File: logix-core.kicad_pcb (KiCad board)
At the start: 6 copper layers, 76 parts, among them J1 QSH-030-01-X-D-A-XX, J2 QSH-030-01-X-D-A-XX, J3 878321420, U1 XC7A15T-CSG325, U1 XC7A15T-FTG256, U2 MP5470GL-0000-P, U3 TPUSBLC6-4SC6, U4 FT230XQ, U5 MX25L3233FZN, U6 XC7A15T-CSG325, U8 MT41K256M16TW-107:P

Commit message: more ddr3, rules and stuff
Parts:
- R17: value R -> 100; footprint Resistor_SMD:R_0402_1005Metric_Pad0.72x0.64mm_HandSolder -> Capacitor_SMD:C_0402_1005Metric
- U1: value XC7A15T-FTG256 -> XC7A15T-CSG325; footprint Package_BGA:Xilinx_FTG256 -> Package_BGA:Xilinx_CSG325
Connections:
- R17 pad 1: /FPGA/DO.DO6+ -> +V1P2
- R17 pad 2: unconnected-(R17-Pad2) -> Net-(U1D-MGTRREF_216)
- U1 pad A10: unconnected-(U1A-IO_L3N_T0_DQS_AD1N_15-PadA10) -> (no net)
- U1 pad A12: unconnected-(U1A-IO_L5N_T0_AD9N_15-PadA12) -> (no net)
- U1 pad A13: unconnected-(U1A-IO_L7P_T1_AD2P_15-PadA13) -> (no net)
- U1 pad A14: unconnected-(U1A-IO_L7N_T1_AD2N_15-PadA14) -> (no net)
- U1 pad A15: unconnected-(U1A-IO_L9N_T1_DQS_AD3N_15-PadA15) -> (no net)
- U1 pad A16: unconnected-(U1A-VCCO_15-PadA16) -> (no net)
- U1 pad A2: (no net) -> +V1P2
- U1 pad A6: (no net) -> Net-(U1D-MGTRREF_216)
- U1 pad A8: unconnected-(U1A-IO_L2P_T0_AD8P_15-PadA8) -> (no net)
- U1 pad A9: unconnected-(U1A-IO_L2N_T0_AD8N_15-PadA9) -> (no net)
- U1 pad B10: unconnected-(U1A-IO_L4P_T0_15-PadB10) -> (no net)
- U1 pad B11: unconnected-(U1A-IO_L4N_T0_15-PadB11) -> (no net)
- U1 pad B12: unconnected-(U1A-IO_L5P_T0_AD9P_15-PadB12) -> (no net)
- U1 pad B13: unconnected-(U1A-VCCO_15-PadB13) -> (no net)
- U1 pad B14: unconnected-(U1A-IO_L8N_T1_AD10N_15-PadB14) -> (no net)
- U1 pad B15: unconnected-(U1A-IO_L9P_T1_DQS_AD3P_15-PadB15) -> (no net)
- U1 pad B16: unconnected-(U1A-IO_L10N_T1_AD11N_15-PadB16) -> (no net)
- U1 pad B4: (no net) -> +V1P0
- U1 pad B9: unconnected-(U1A-IO_L3P_T0_DQS_AD1P_15-PadB9) -> (no net)
- U1 pad C1: (no net) -> +V1P2
- U1 pad C10: unconnected-(U1A-VCCO_15-PadC10) -> (no net)
- U1 pad C11: unconnected-(U1A-IO_L11P_T1_SRCC_15-PadC11) -> (no net)
- U1 pad C12: unconnected-(U1A-IO_L11N_T1_SRCC_15-PadC12) -> (no net)
- U1 pad C13: unconnected-(U1A-IO_L12N_T1_MRCC_15-PadC13) -> (no net)
- U1 pad C14: unconnected-(U1A-IO_L8P_T1_AD10P_15-PadC14) -> (no net)
- U1 pad C16: unconnected-(U1A-IO_L10P_T1_AD11P_15-PadC16) -> (no net)
- U1 pad C5: (no net) -> +V1P0
- U1 pad C8: unconnected-(U1A-IO_L1P_T0_AD0P_15-PadC8) -> (no net)
- U1 pad C9: unconnected-(U1A-IO_L1N_T0_AD0N_15-PadC9) -> (no net)
- U1 pad D10: unconnected-(U1A-IO_0_15-PadD10) -> (no net)
- U1 pad D11: unconnected-(U1A-IO_L14N_T2_SRCC_15-PadD11) -> (no net)
- U1 pad D13: unconnected-(U1A-IO_L12P_T1_MRCC_15-PadD13) -> (no net)
- U1 pad D14: unconnected-(U1A-IO_L15P_T2_DQS_15-PadD14) -> (no net)
- U1 pad D15: unconnected-(U1A-IO_L15N_T2_DQS_ADV_B_15-PadD15) -> (no net)
- U1 pad D16: unconnected-(U1A-IO_L17N_T2_A25_15-PadD16) -> (no net)
- U1 pad D8: unconnected-(U1A-IO_L6P_T0_15-PadD8) -> (no net)
- U1 pad D9: unconnected-(U1A-IO_L6N_T0_VREF_15-PadD9) -> (no net)
- U1 pad E1: (no net) -> +V1P2
- U1 pad E11: unconnected-(U1A-IO_L14P_T2_SRCC_15-PadE11) -> (no net)
- U1 pad E12: unconnected-(U1A-IO_L13P_T2_MRCC_15-PadE12) -> (no net)
- U1 pad E13: unconnected-(U1A-IO_L13N_T2_MRCC_15-PadE13) -> (no net)
- U1 pad E14: unconnected-(U1A-VCCO_15-PadE14) -> (no net)
- U1 pad E15: unconnected-(U1A-IO_L18N_T2_A23_15-PadE15) -> (no net)
- U1 pad E16: unconnected-(U1A-IO_L17P_T2_A26_15-PadE16) -> (no net)
- U1 pad E5: (no net) -> +V1P0
- U1 pad E7: unconnected-(U1C-CFGBVS_0-PadE7) -> (no net)
- U1 pad E8: /FPGA/FPGA pg.3/INT_FLASH_SPI_CLK -> (no net)
- U1 pad F12: unconnected-(U1A-IO_L16P_T2_A28_15-PadF12) -> (no net)
- U1 pad F13: unconnected-(U1A-IO_L16N_T2_A27_15-PadF13) -> (no net)
- U1 pad F14: unconnected-(U1A-IO_L21N_T3_DQS_A18_15-PadF14) -> (no net)
- U1 pad F15: unconnected-(U1A-IO_L18P_T2_A24_15-PadF15) -> (no net)
- U1 pad F3: (no net) -> +V1P2
- U1 pad F5: (no net) -> +V1P0
- U1 pad G11: unconnected-(U1A-IO_25_15-PadG11) -> (no net)
- U1 pad G12: unconnected-(U1A-IO_L19N_T3_A21_VREF_15-PadG12) -> (no net)
- U1 pad G14: unconnected-(U1A-IO_L21P_T3_DQS_15-PadG14) -> (no net)
- U1 pad G15: unconnected-(U1A-IO_L24N_T3_RS0_15-PadG15) -> (no net)
- U1 pad G16: unconnected-(U1A-IO_L22N_T3_A16_15-PadG16) -> (no net)
- U1 pad G2: (no net) -> +V1P2
- U1 pad H10: unconnected-(U1C-DONE_0-PadH10) -> (no net)
- U1 pad H11: unconnected-(U1A-IO_L19P_T3_A22_15-PadH11) -> (no net)
- U1 pad H12: unconnected-(U1A-IO_L20P_T3_A20_15-PadH12) -> (no net)
- U1 pad H13: unconnected-(U1A-IO_L20N_T3_A19_15-PadH13) -> (no net)
- U1 pad H14: unconnected-(U1A-IO_L24P_T3_RS1_15-PadH14) -> (no net)
- U1 pad H15: unconnected-(U1A-VCCO_15-PadH15) -> (no net)
- U1 pad H16: unconnected-(U1A-IO_L22P_T3_A17_15-PadH16) -> (no net)
- U1 pad H7: unconnected-(U1C-VREFN_0-PadH7) -> (no net)
- U1 pad H8: unconnected-(U1C-VP_0-PadH8) -> (no net)
- U1 pad J12: unconnected-(U1A-VCCO_15-PadJ12) -> (no net)
- U1 pad J13: /FPGA/FPGA pg.1/INT_FLASH_SPI_D0 -> (no net)
- U1 pad J14: /FPGA/FPGA pg.1/INT_FLASH_SPI_D1 -> (no net)
- U1 pad J15: unconnected-(U1A-IO_L23P_T3_FOE_B_15-PadJ15) -> (no net)
- U1 pad J16: unconnected-(U1A-IO_L23N_T3_FWE_B_15-PadJ16) -> (no net)
- U1 pad J7: unconnected-(U1C-VN_0-PadJ7) -> (no net)
- U1 pad J8: unconnected-(U1C-VREFP_0-PadJ8) -> (no net)
- U1 pad K10: unconnected-(U1C-INIT_B_0-PadK10) -> (no net)
- U1 pad K12: unconnected-(U1A-IO_0_14-PadK12) -> (no net)
- U1 pad K13: unconnected-(U1A-IO_L5P_T0_D06_14-PadK13) -> (no net)
- U1 pad K15: /FPGA/FPGA pg.1/INT_FLASH_SPI_D2 -> (no net)
- U1 pad K16: /FPGA/FPGA pg.1/INT_FLASH_SPI_D3 -> (no net)
- U1 pad K7: unconnected-(U1C-DXN_0-PadK7) -> (no net)
- U1 pad K8: unconnected-(U1C-DXP_0-PadK8) -> (no net)
- U1 pad L12: /FPGA/FPGA pg.1/INT_FLASH_SPI_CS# -> (no net)
- U1 pad L13: unconnected-(U1A-IO_L5N_T0_D07_14-PadL13) -> (no net)
- U1 pad L14: unconnected-(U1A-IO_L4P_T0_D04_14-PadL14) -> (no net)
- U1 pad L15: unconnected-(U1A-IO_L3P_T0_DQS_PUDC_B_14-PadL15) -> (no net)
- U1 pad L16: unconnected-(U1A-VCCO_14-PadL16) -> (no net)
- U1 pad L6: unconnected-(U1C-VCCO_0-PadL6) -> (no net)
- U1 pad L7: /FPGA/FPGA pg.3/JTAG.TCK -> (no net)
- U1 pad L9: unconnected-(U1C-PROGRAM_B_0-PadL9) -> (no net)
- U1 pad M10: unconnected-(U1C-M1_0-PadM10) -> (no net)
- U1 pad M11: unconnected-(U1C-M2_0-PadM11) -> (no net)
- U1 pad M12: unconnected-(U1A-IO_L6N_T0_D08_VREF_14-PadM12) -> (no net)
- U1 pad M13: unconnected-(U1A-VCCO_14-PadM13) -> (no net)
- U1 pad M14: unconnected-(U1A-IO_L4N_T0_D05_14-PadM14) -> (no net)
- U1 pad M15: unconnected-(U1A-IO_L3N_T0_DQS_EMCCLK_14-PadM15) -> (no net)
- U1 pad M16: unconnected-(U1A-IO_L7P_T1_D09_14-PadM16) -> (no net)
- U1 pad M6: unconnected-(U1A-IO_L19P_T3_A10_D26_14-PadM6) -> (no net)
- U1 pad M7: /FPGA/FPGA pg.3/JTAG.TMS -> (no net)
- U1 pad M9: unconnected-(U1C-M0_0-PadM9) -> (no net)
- U1 pad N10: unconnected-(U1A-VCCO_14-PadN10) -> (no net)
- U1 pad N11: unconnected-(U1A-IO_L13P_T2_MRCC_14-PadN11) -> (no net)
- U1 pad N12: unconnected-(U1A-IO_L13N_T2_MRCC_14-PadN12) -> (no net)
- U1 pad N13: unconnected-(U1A-IO_L11P_T1_SRCC_14-PadN13) -> (no net)
- U1 pad N14: unconnected-(U1A-IO_L12P_T1_MRCC_14-PadN14) -> (no net)
- U1 pad N16: unconnected-(U1A-IO_L7N_T1_D10_14-PadN16) -> (no net)
- U1 pad N6: unconnected-(U1A-IO_L19N_T3_A09_D25_VREF_14-PadN6) -> (no net)
- U1 pad N7: /FPGA/FPGA pg.3/JTAG.TDI -> (no net)
- U1 pad N8: /FPGA/FPGA pg.3/JTAG.TDO -> (no net)
- U1 pad N9: unconnected-(U1A-IO_L18P_T2_A12_D28_14-PadN9) -> (no net)
- U1 pad P10: unconnected-(U1A-IO_L14P_T2_SRCC_14-PadP10) -> (no net)
- U1 pad P11: unconnected-(U1A-IO_L14N_T2_SRCC_14-PadP11) -> (no net)
- U1 pad P13: unconnected-(U1A-IO_L11N_T1_SRCC_14-PadP13) -> (no net)
- U1 pad P14: unconnected-(U1A-IO_L12N_T1_MRCC_14-PadP14) -> (no net)
- U1 pad P15: unconnected-(U1A-IO_L8P_T1_D11_14-PadP15) -> (no net)
- U1 pad P16: unconnected-(U1A-IO_L8N_T1_D12_14-PadP16) -> (no net)
- U1 pad P6: unconnected-(U1A-IO_25_14-PadP6) -> (no net)
- U1 pad P7: unconnected-(U1A-VCCO_14-PadP7) -> (no net)
- U1 pad P8: unconnected-(U1A-IO_L20P_T3_A08_D24_14-PadP8) -> (no net)
- U1 pad P9: unconnected-(U1A-IO_L18N_T2_A11_D27_14-PadP9) -> (no net)
- U1 pad R10: unconnected-(U1A-IO_L17P_T2_A14_D30_14-PadR10) -> (no net)
- U1 pad R11: unconnected-(U1A-IO_L17N_T2_A13_D29_14-PadR11) -> (no net)
- U1 pad R12: unconnected-(U1A-IO_L15P_T2_DQS_RDWR_B_14-PadR12) -> (no net)
- U1 pad R13: unconnected-(U1A-IO_L16P_T2_CSI_B_14-PadR13) -> (no net)
- U1 pad R14: unconnected-(U1A-VCCO_14-PadR14) -> (no net)
- U1 pad R15: unconnected-(U1A-IO_L9P_T1_DQS_14-PadR15) -> (no net)
- U1 pad R16: unconnected-(U1A-IO_L9N_T1_DQS_D13_14-PadR16) -> (no net)
- U1 pad R5: unconnected-(U1A-IO_L23P_T3_A03_D19_14-PadR5) -> (no net)
- U1 pad R6: unconnected-(U1A-IO_L24P_T3_A01_D17_14-PadR6) -> (no net)
- U1 pad R7: unconnected-(U1A-IO_L24N_T3_A00_D16_14-PadR7) -> (no net)
- U1 pad R8: unconnected-(U1A-IO_L20N_T3_A07_D23_14-PadR8) -> (no net)
- U1 pad T10: unconnected-(U1A-IO_L22N_T3_A04_D20_14-PadT10) -> (no net)
- U1 pad T11: unconnected-(U1A-VCCO_14-PadT11) -> (no net)
- U1 pad T12: unconnected-(U1A-IO_L15N_T2_DQS_DOUT_CSO_B_14-PadT12) -> (no net)
- U1 pad T13: unconnected-(U1A-IO_L16N_T2_A15_D31_14-PadT13) -> (no net)
- U1 pad T14: unconnected-(U1A-IO_L10P_T1_D14_14-PadT14) -> (no net)
- U1 pad T15: unconnected-(U1A-IO_L10N_T1_D15_14-PadT15) -> (no net)
- U1 pad T5: unconnected-(U1A-IO_L23N_T3_A02_D18_14-PadT5) -> (no net)
- U1 pad T7: unconnected-(U1A-IO_L21P_T3_DQS_14-PadT7) -> (no net)
- U1 pad T8: unconnected-(U1A-IO_L21N_T3_DQS_A06_D22_14-PadT8) -> (no net)
- U1 pad T9: unconnected-(U1A-IO_L22P_T3_A05_D21_14-PadT9) -> (no net)
- U6 pad M4: /DDR3_ADDR3 -> unconnected-(U6B-IO_L10P_T1_34-PadM4)
- U6 pad N1: /DDR3_ADDR1 -> unconnected-(U6B-IO_L9P_T1_DQS_34-PadN1)
- U6 pad N2: /DDR3_ADDR6 -> unconnected-(U6B-IO_L11N_T1_SRCC_34-PadN2)
- U6 pad N3: /DDR3_ADDR5 -> unconnected-(U6B-IO_L11P_T1_SRCC_34-PadN3)
- U6 pad N4: /DDR3_ADDR4 -> unconnected-(U6B-IO_L10N_T1_34-PadN4)
- U6 pad N6: /DDR3_ADDR0 -> unconnected-(U6B-IO_L8N_T1_34-PadN6)
- U6 pad P1: /DDR3_ADDR2 -> unconnected-(U6B-IO_L9N_T1_DQS_34-PadP1)
- U6 pad P3: /DDR3_ADDR8 -> /DDR3_ADDR10
- U6 pad P4: /DDR3_ADDR7 -> unconnected-(U6B-IO_L12P_T1_MRCC_34-PadP4)
- U6 pad P5: /DDR3_BLOCK_ADDR2 -> unconnected-(U6B-IO_L19N_T3_VREF_34-PadP5)
- U6 pad P6: /DDR3_BLOCK_ADDR1 -> unconnected-(U6B-IO_L19P_T3_34-PadP6)
- U6 pad R1: /DDR3_ADDR10 -> unconnected-(U6B-IO_L13N_T2_MRCC_34-PadR1)
- U6 pad R2: /DDR3_ADDR9 -> /DDR3_BLOCK_ADDR1
- U6 pad R3: /DDR3_ADDR11 -> /DDR3_ADDR12
- U6 pad T2: /DDR3_ADDR12 -> /DDR3_ADDR4
- U6 pad T3: /DDR3_RESET# -> /DDR3_ADDR6
- U6 pad T4: /DDR3_RAS# -> /DDR3_ADDR8
- U6 pad U1: /DDR3_ADDR14 -> /DDR3_ADDR1
- U6 pad U2: /DDR3_ADDR13 -> /DDR3_ADDR11
- U6 pad U4: /DDR3_WE# -> unconnected-(U6B-IO_L18P_T2_34-PadU4)
- U6 pad U5: /DDR3_CLK- -> /DDR3_ADDR0
- U6 pad U6: /DDR3_CLK+ -> /DDR3_ADDR5
- U6 pad V2: /DDR3_CS# -> /DDR3_ADDR14
- U6 pad V3: /DDR3_CAS# -> /DDR3_BLOCK_ADDR0
- U6 pad V4: /DDR3_BLOCK_ADDR0 -> /DDR3_ADDR3
- U6 pad V6: /DDR3_LDQS- -> /DDR3_ADDR2
- U6 pad V7: /DDR3_UDQS- -> /DDR3_ADDR7
- U6 pad V8: /DDR3_UDQS+ -> /DDR3_ADDR9
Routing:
- net (no net): track 67.2 -> 148.5 mm, vias 97 -> 212
- net +V1P2: track 0.00 -> 23.3 mm, vias 0 -> 33
- net GND: track 75.4 -> 54.2 mm, vias 126 -> 96
- net /DDR3_ADDR7: track 1.13 -> 19.3 mm
- net /DDR3_ADDR9: track 4.61 -> 19.1 mm
- net /DDR3_ADDR5: track 5.49 -> 18.5 mm
- net /DDR3_ADDR2: track 4.61 -> 17.5 mm
- net /DDR3_ADDR0: track 5.17 -> 17.2 mm
- net /DDR3_ADDR1: track 19.5 -> 7.61 mm
- net /DDR3_ADDR11: track 20.2 -> 8.55 mm
- net /DDR3_ADDR14: track 19.9 -> 8.46 mm
- net /DDR3_ADDR3: track 6.05 -> 17.0 mm
- net /DDR3/ZQ: track 12.9 -> 2.86 mm
- net /DDR3_DQ2: track 1.13 -> 11.1 mm
- net /DDR3_DQ15: track 4.61 -> 12.0 mm
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
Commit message: more ddr3
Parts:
- moved U8 5.02 mm to (161.0, 144.0)
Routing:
- net /DDR3_DQ3: track 2.46 -> 25.5 mm
- net /DDR3_DQ14: track 2.49 -> 25.3 mm
- net /DDR3_DQ5: track 3.43 -> 25.6 mm
- net /DDR3_DQ8: track 4.18 -> 25.6 mm
- net /DDR3_DQ10: track 4.26 -> 25.6 mm
- net /DDR3_DQ1: track 7.55 -> 26.0 mm
- net /DDR3_DQ13: track 8.31 -> 20.3 mm, vias 2 -> 1
- net /DDR3_DQ11: track 11.7 -> 22.6 mm
- net /DDR3_DQ2: track 11.1 -> 1.13 mm
- net /DDR3_DQ9: track 9.57 -> 1.13 mm
- net /DDR3_DQ12: track 7.41 -> 15.3 mm
- net /DDR3_DQ15: track 12.0 -> 18.7 mm, vias 2 -> 1
- net /DDR3_DQ6: track 7.26 -> 1.13 mm
- net unconnected-(U6B-IO_L8N_T1_34-PadN6): track 6.35 -> 0.57 mm
- net /DDR3_DQ0: track 6.46 -> 1.70 mm
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
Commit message: wip rickard
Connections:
- U6 pad J4: /DDR3_DQ4 -> /DDR3_DQ13
- U6 pad J5: /DDR3_DQ3 -> /DDR3_DQ15
- U6 pad J6: /DDR3_DQ0 -> /DDR3_DQ12
- U6 pad K1: /DDR3_DQ6 -> /DDR3_DQ1
- U6 pad K2: /DDR3_DQ5 -> /DDR3_DQ10
- U6 pad K3: /DDR3_DQ7 -> /DDR3_DQ14
- U6 pad K5: /DDR3_DQ2 -> /DDR3_DQ0
- U6 pad K6: /DDR3_DQ1 -> /DDR3_DQ11
- U6 pad L3: /DDR3_DQ10 -> /DDR3_DQ6
- U6 pad L4: /DDR3_DQ9 -> /DDR3_DQ3
- U6 pad L5: /DDR3_DQ11 -> /DDR3_DQ2
- U6 pad M1: /DDR3_DQ14 -> /DDR3_DQ7
- U6 pad M2: /DDR3_DQ13 -> /DDR3_DQ9
- U6 pad M4: unconnected-(U6B-IO_L10P_T1_34-PadM4) -> /DDR3_RESET#
- U6 pad M5: /DDR3_DQ12 -> /DDR3_DQ5
- U6 pad M6: /DDR3_DQ15 -> /DDR3_DQ4
- U6 pad N1: unconnected-(U6B-IO_L9P_T1_DQS_34-PadN1) -> /DDR3_ADDR13
- U6 pad N2: unconnected-(U6B-IO_L11N_T1_SRCC_34-PadN2) -> /DDR3_CLK-
- U6 pad N3: unconnected-(U6B-IO_L11P_T1_SRCC_34-PadN3) -> /DDR3_CS#
- U6 pad N4: unconnected-(U6B-IO_L10N_T1_34-PadN4) -> /DDR3_WE#
- U6 pad N6: unconnected-(U6B-IO_L8N_T1_34-PadN6) -> /DDR3_RAS#
- U6 pad P1: unconnected-(U6B-IO_L9N_T1_DQS_34-PadP1) -> /DDR3_CAS#
- U6 pad P4: unconnected-(U6B-IO_L12P_T1_MRCC_34-PadP4) -> /DDR3_CLK+
- U6 pad P5: unconnected-(U6B-IO_L19N_T3_VREF_34-PadP5) -> /DDR3_UDQS-
- U6 pad P6: unconnected-(U6B-IO_L19P_T3_34-PadP6) -> /DDR3_UDQS+
- U6 pad R1: unconnected-(U6B-IO_L13N_T2_MRCC_34-PadR1) -> /DDR3_LDQS-
- U6 pad U4: unconnected-(U6B-IO_L18P_T2_34-PadU4) -> /DDR3_BLOCK_ADDR2
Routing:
- net /DDR3_DQ4: track 1.70 -> 25.2 mm
- net /DDR3_DQ0: track 1.70 -> 25.1 mm
- net /DDR3_DQ7: track 1.70 -> 24.5 mm
- net /DDR3_DQ9: track 1.13 -> 23.5 mm
- net /DDR3_DQ6: track 1.13 -> 23.3 mm
- net /DDR3_DQ2: track 1.13 -> 21.9 mm
- net /DDR3_DQ12: track 15.3 -> 24.6 mm
- net /DDR3_UDQS+: track 2.71 -> 10.2 mm, vias 1 -> 2
- net /DDR3_UDQS-: track 2.72 -> 9.29 mm, vias 1 -> 2
- net /DDR3_DQ15: track 18.7 -> 24.6 mm, vias 1 -> 2
- net unconnected-(U6B-IO_L19P_T3_34-PadP6): track 4.82 -> 0.00 mm, vias 1 -> 0
- net unconnected-(U6B-IO_L19N_T3_VREF_34-PadP5): track 3.94 -> 0.00 mm, vias 1 -> 0
- net /DDR3_DQ5: track 25.6 -> 21.8 mm
- net /DDR3_BLOCK_ADDR2: track 7.20 -> 10.8 mm, vias 1 -> 2
- net unconnected-(U6B-IO_L18P_T2_34-PadU4): track 3.57 -> 0.00 mm, vias 1 -> 0
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
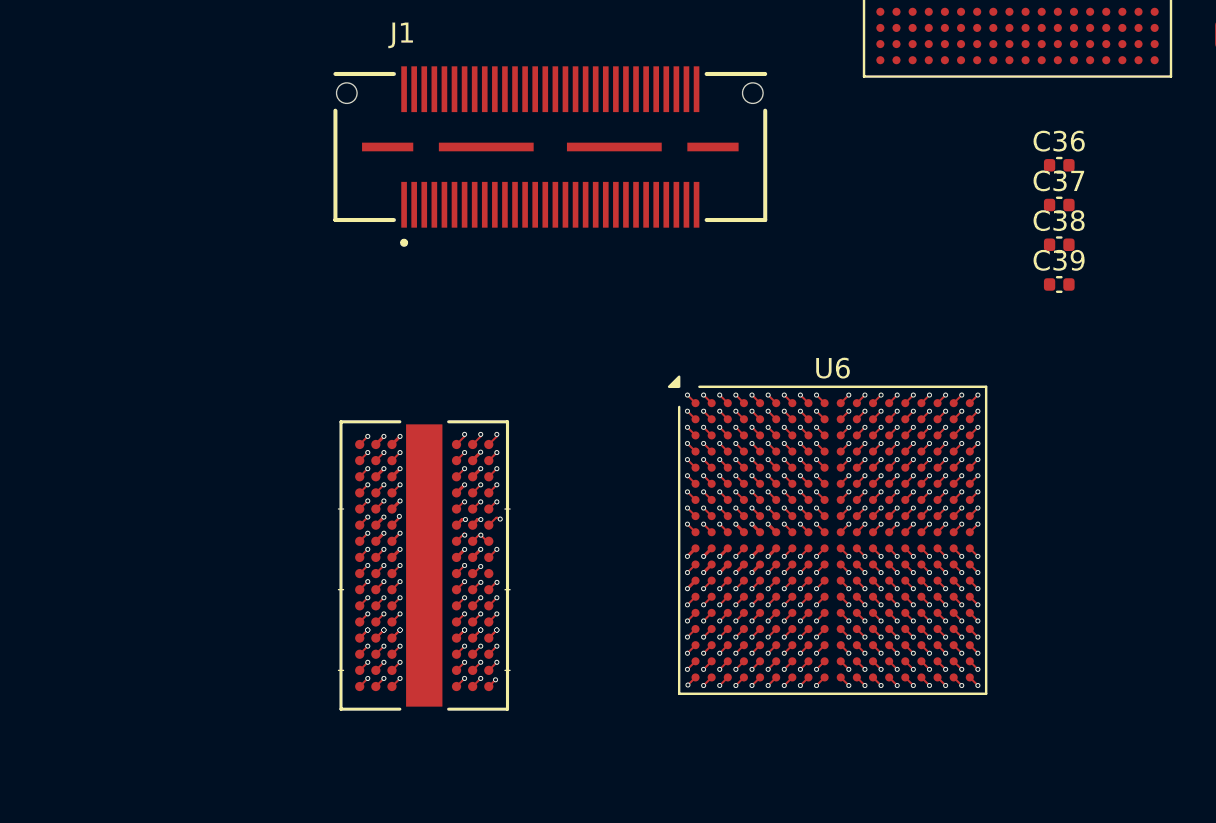
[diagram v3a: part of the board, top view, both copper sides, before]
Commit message: changed ddr3 pinning according to hard-ip in vivado
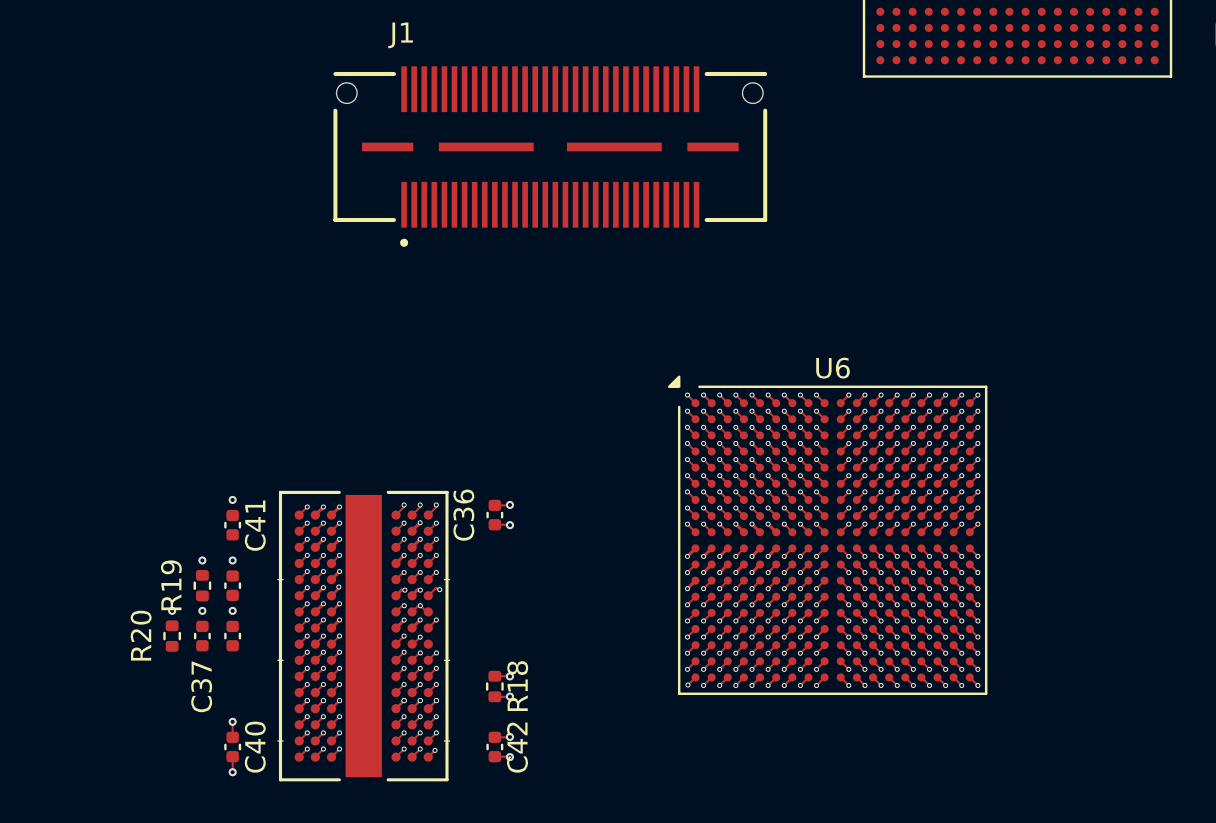
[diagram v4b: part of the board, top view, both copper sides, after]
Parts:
- added C40: 1u, Capacitor_SMD:C_0402_1005Metric, F.Cu at (151.5, 153.0)
- added C41: 1u, Capacitor_SMD:C_0402_1005Metric, F.Cu at (151.5, 142.0)
- added C42: 1u, Capacitor_SMD:C_0402_1005Metric, F.Cu at (164.5, 153.0)
- added R18: 240, Resistor_SMD:R_0402_1005Metric, F.Cu at (164.5, 150.0)
- added R19: 1k, Resistor_SMD:R_0402_1005Metric, F.Cu at (150.0, 145.0)
- added R20: 1k, Resistor_SMD:R_0402_1005Metric, F.Cu at (148.5, 147.5)
- moved C37 47.6 mm to (150.0, 147.5), turned to -90 degrees
- moved C38 45.3 mm to (151.5, 147.5), turned to -90 degrees
- moved C39 43.6 mm to (151.5, 145.0), turned to -90 degrees
- moved C36 32.9 mm to (164.5, 141.5), turned to -90 degrees
- moved U8 4.61 mm to (158.0, 147.5)
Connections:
- U6 pad A10: /DI.DI5- -> /DDR3_DQ6
- U6 pad A12: /DI.DI7- -> /DDR3_DQ8
- U6 pad A13: /DI.DI8+ -> /DDR3_DQ9
- U6 pad A14: /DI.DI8- -> /DDR3_DQ10
- U6 pad A15: /DI.DI10- -> /DDR3_DQ12
- U6 pad A17: /DI.DI15- -> unconnected-(U6A-IO_L15N_T2_DQS_ADV_B_15-PadA17)
- U6 pad A9: /DI.DI3- -> /DDR3_LDQS-
- U6 pad B10: /DI.DI5+ -> /DDR3_DQ5
- U6 pad B11: /DI.DI4- -> /DDR3_DQ4
- U6 pad B12: /DI.DI7+ -> /DDR3_UDM
- U6 pad B14: /DI.DI10+ -> /DDR3_DQ11
- U6 pad B15: /DI.DI9- -> /DDR3_UDQS-
- U6 pad B16: /DI.DI15+ -> unconnected-(U6A-IO_L15P_T2_DQS_15-PadB16)
- U6 pad B17: /DI.DI16- -> unconnected-(U6A-IO_L16N_T2_A27_15-PadB17)
- U6 pad B9: /DI.DI3+ -> /DDR3_LDQS+
- U6 pad C11: /DI.DI4+ -> /DDR3_DQ3
- U6 pad C12: /DI.DI6- -> unconnected-(U6A-IO_L6N_T0_VREF_15-PadC12)
- U6 pad C13: /DI.DI11- -> /DDR3_DQ14
- U6 pad C14: /DI.DI9+ -> /DDR3_UDQS+
- U6 pad C16: /DI.DI16+ -> unconnected-(U6A-IO_L16P_T2_A28_15-PadC16)
- U6 pad C8: /DI.DI1- -> /DDR3_DQ0
- U6 pad C9: /DI.DI2- -> /DDR3_DQ2
- U6 pad D11: /DI.DI6+ -> /DDR3_DQ7
- U6 pad D13: /DI.DI11+ -> /DDR3_DQ13
- U6 pad D14: /DI.DI12- -> /DDR3_RESET#
- U6 pad D15: /DI.DI13- -> unconnected-(U6A-IO_L13N_T2_MRCC_15-PadD15)
- U6 pad D16: /DI.DI14- -> unconnected-(U6A-IO_L14N_T2_SRCC_15-PadD16)
- U6 pad D8: /DI.DI1+ -> /DDR3_LDM
- U6 pad D9: /DI.DI2+ -> /DDR3_DQ1
- U6 pad E13: /DI.DI12+ -> /DDR3_DQ15
- U6 pad E15: /DI.DI13+ -> unconnected-(U6A-IO_L13P_T2_MRCC_15-PadE15)
- U6 pad E16: /DI.DI14+ -> unconnected-(U6A-IO_L14P_T2_SRCC_15-PadE16)
- U6 pad J14: /DO.DO3+ -> unconnected-(U6A-IO_L5P_T0_D06_14-PadJ14)
- U6 pad J18: /DO.DO1+ -> unconnected-(U6A-IO_L3P_T0_DQS_PUDC_B_14-PadJ18)
- U6 pad J4: /DDR3_DQ13 -> unconnected-(U6B-IO_L2N_T0_34-PadJ4)
- U6 pad J5: /DDR3_DQ15 -> unconnected-(U6B-IO_L2P_T0_34-PadJ5)
- U6 pad J6: /DDR3_DQ12 -> unconnected-(U6B-IO_0_34-PadJ6)
- U6 pad K1: /DDR3_DQ1 -> unconnected-(U6B-IO_L3N_T0_DQS_34-PadK1)
- U6 pad K15: /DO.DO3- -> unconnected-(U6A-IO_L5N_T0_D07_14-PadK15)
- U6 pad K17: /DO.DO2+ -> unconnected-(U6A-IO_L4P_T0_D04_14-PadK17)
- U6 pad K18: /DO.DO1- -> unconnected-(U6A-IO_L3N_T0_DQS_EMCCLK_14-PadK18)
- U6 pad K2: /DDR3_DQ10 -> unconnected-(U6B-IO_L3P_T0_DQS_34-PadK2)
- U6 pad K3: /DDR3_DQ14 -> unconnected-(U6B-IO_L4P_T0_34-PadK3)
- U6 pad K5: /DDR3_DQ0 -> unconnected-(U6B-IO_L1N_T0_34-PadK5)
- U6 pad K6: /DDR3_DQ11 -> unconnected-(U6B-IO_L1P_T0_34-PadK6)
- U6 pad L18: /DO.DO2- -> unconnected-(U6A-IO_L4N_T0_D05_14-PadL18)
- U6 pad L2: /DDR3_DQ8 -> unconnected-(U6B-IO_L4N_T0_34-PadL2)
- U6 pad L3: /DDR3_DQ6 -> unconnected-(U6B-IO_L5N_T0_34-PadL3)
- U6 pad L4: /DDR3_DQ3 -> unconnected-(U6B-IO_L5P_T0_34-PadL4)
- U6 pad L5: /DDR3_DQ2 -> unconnected-(U6B-IO_L6P_T0_34-PadL5)
- U6 pad M1: /DDR3_DQ7 -> unconnected-(U6B-IO_L7N_T1_34-PadM1)
- U6 pad M14: /DO.DO5+ -> /DDR3_ADDR12
- U6 pad M16: /DO.DO4+ -> /DDR3_ADDR14
- U6 pad M17: /DO.DO4- -> /DDR3_ADDR13
- U6 pad M2: /DDR3_DQ9 -> unconnected-(U6B-IO_L7P_T1_34-PadM2)
- U6 pad M4: /DDR3_RESET# -> unconnected-(U6B-IO_L10P_T1_34-PadM4)
- U6 pad M5: /DDR3_DQ5 -> unconnected-(U6B-IO_L6N_T0_VREF_34-PadM5)
- U6 pad M6: /DDR3_DQ4 -> unconnected-(U6B-IO_L8P_T1_34-PadM6)
- U6 pad N1: /DDR3_ADDR13 -> unconnected-(U6B-IO_L9P_T1_DQS_34-PadN1)
- U6 pad N14: /DO.DO5- -> /DDR3_ADDR11
- U6 pad N16: /DO.DO6+ -> /DDR3_ADDR10
- U6 pad N17: /DO.DO6- -> /DDR3_ADDR9
- U6 pad N18: /DO.DO7+ -> /DDR3_ADDR8
- U6 pad N2: /DDR3_CLK- -> unconnected-(U6B-IO_L11N_T1_SRCC_34-PadN2)
- U6 pad N3: /DDR3_CS# -> unconnected-(U6B-IO_L11P_T1_SRCC_34-PadN3)
- U6 pad N4: /DDR3_WE# -> unconnected-(U6B-IO_L10N_T1_34-PadN4)
- U6 pad N6: /DDR3_RAS# -> unconnected-(U6B-IO_L8N_T1_34-PadN6)
- U6 pad P1: /DDR3_CAS# -> unconnected-(U6B-IO_L9N_T1_DQS_34-PadP1)
- U6 pad P14: unconnected-(U6A-IO_L12P_T1_MRCC_14-PadP14) -> /DDR3_ADDR4
- U6 pad P15: /DO.DO8+ -> /DDR3_ADDR6
- U6 pad P16: /DO.DO8- -> /DDR3_ADDR5
- U6 pad P18: /DO.DO7- -> /DDR3_ADDR7
- U6 pad P3: /DDR3_ADDR10 -> unconnected-(U6B-IO_L12N_T1_MRCC_34-PadP3)
- U6 pad P4: /DDR3_CLK+ -> unconnected-(U6B-IO_L12P_T1_MRCC_34-PadP4)
- U6 pad P5: /DDR3_UDQS- -> unconnected-(U6B-IO_L19N_T3_VREF_34-PadP5)
- U6 pad P6: /DDR3_UDQS+ -> unconnected-(U6B-IO_L19P_T3_34-PadP6)
- U6 pad R1: /DDR3_LDQS- -> unconnected-(U6B-IO_L13N_T2_MRCC_34-PadR1)
- U6 pad R13: unconnected-(U6A-IO_L19P_T3_A10_D26_14-PadR13) -> /DDR3_CLK_EN
- U6 pad R15: unconnected-(U6A-IO_L12N_T1_MRCC_14-PadR15) -> /DDR3_ADDR3
- U6 pad R16: unconnected-(U6A-IO_L14P_T2_SRCC_14-PadR16) -> /DDR3_ADDR2
- U6 pad R17: unconnected-(U6A-IO_L14N_T2_SRCC_14-PadR17) -> /DDR3_ADDR1
- U6 pad R18: unconnected-(U6A-IO_L15P_T2_DQS_RDWR_B_14-PadR18) -> /DDR3_ADDR0
- U6 pad R2: /DDR3_BLOCK_ADDR1 -> unconnected-(U6B-IO_L13P_T2_MRCC_34-PadR2)
- U6 pad R3: /DDR3_ADDR12 -> unconnected-(U6B-IO_L14P_T2_SRCC_34-PadR3)
- U6 pad R5: /DDR3_CLK_EN -> unconnected-(U6B-IO_L21P_T3_DQS_34-PadR5)
- U6 pad R7: /DDR3_ODT -> unconnected-(U6B-IO_L22P_T3_34-PadR7)
- U6 pad T17: unconnected-(U6A-IO_L16P_T2_CSI_B_14-PadT17) -> /DDR3_BLOCK_ADDR1
- U6 pad T18: unconnected-(U6A-IO_L15N_T2_DQS_DOUT_CSO_B_14-PadT18) -> /DDR3_BLOCK_ADDR2
- U6 pad T2: /DDR3_ADDR4 -> unconnected-(U6B-IO_L14N_T2_SRCC_34-PadT2)
- U6 pad T3: /DDR3_ADDR6 -> unconnected-(U6B-IO_L17N_T2_34-PadT3)
- U6 pad T4: /DDR3_ADDR8 -> unconnected-(U6B-IO_L17P_T2_34-PadT4)
- U6 pad T5: /DDR3_LDM -> unconnected-(U6B-IO_L21N_T3_DQS_34-PadT5)
- U6 pad T7: /DDR3_UDM -> unconnected-(U6B-IO_L22N_T3_34-PadT7)
- U6 pad U1: /DDR3_ADDR1 -> unconnected-(U6B-IO_L15N_T2_DQS_34-PadU1)
- U6 pad U14: unconnected-(U6A-IO_L20P_T3_A08_D24_14-PadU14) -> /DDR3_ODT
- U6 pad U15: unconnected-(U6A-IO_L17P_T2_A14_D30_14-PadU15) -> /DDR3_RAS#
- U6 pad U16: unconnected-(U6A-IO_L17N_T2_A13_D29_14-PadU16) -> /DDR3_CAS#
- U6 pad U17: unconnected-(U6A-IO_L16N_T2_A15_D31_14-PadU17) -> /DDR3_BLOCK_ADDR0
- U6 pad U2: /DDR3_ADDR11 -> unconnected-(U6B-IO_L15P_T2_DQS_34-PadU2)
- U6 pad U4: /DDR3_BLOCK_ADDR2 -> unconnected-(U6B-IO_L18P_T2_34-PadU4)
- U6 pad U5: /DDR3_ADDR0 -> unconnected-(U6B-IO_L20N_T3_34-PadU5)
- U6 pad U6: /DDR3_ADDR5 -> unconnected-(U6B-IO_L20P_T3_34-PadU6)
- U6 pad U7: /DDR3_LDQS+ -> unconnected-(U6B-IO_L23P_T3_34-PadU7)
- U6 pad V12: unconnected-(U6A-IO_L21P_T3_DQS_14-PadV12) -> /DDR3_CLK+
- U6 pad V13: unconnected-(U6A-IO_L21N_T3_DQS_A06_D22_14-PadV13) -> /DDR3_CLK-
- U6 pad V16: unconnected-(U6A-IO_L18P_T2_A12_D28_14-PadV16) -> /DDR3_WE#
- U6 pad V17: unconnected-(U6A-IO_L18N_T2_A11_D27_14-PadV17) -> /DDR3_CS#
- U6 pad V2: /DDR3_ADDR14 -> unconnected-(U6B-IO_L16N_T2_34-PadV2)
- U6 pad V3: /DDR3_BLOCK_ADDR0 -> unconnected-(U6B-IO_L16P_T2_34-PadV3)
- U6 pad V4: /DDR3_ADDR3 -> unconnected-(U6B-IO_L18N_T2_34-PadV4)
- U6 pad V6: /DDR3_ADDR2 -> unconnected-(U6B-IO_L23N_T3_34-PadV6)
- U6 pad V7: /DDR3_ADDR7 -> unconnected-(U6B-IO_L24N_T3_34-PadV7)
- U6 pad V8: /DDR3_ADDR9 -> unconnected-(U6B-IO_L24P_T3_34-PadV8)
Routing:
- net /DDR3_DQ3: track 25.4 -> 1.11 mm
- net /DDR3_DQ4: track 25.2 -> 1.70 mm
- net /DDR3_DQ0: track 25.1 -> 1.70 mm
- net /DDR3_DQ7: track 24.5 -> 1.14 mm
- net /DDR3_DQ1: track 23.7 -> 1.12 mm
- net /DDR3_DQ10: track 23.4 -> 1.13 mm
- net /DDR3_DQ6: track 23.3 -> 1.13 mm
- net /DDR3_DQ2: track 21.9 -> 1.13 mm
- net /DDR3_DQ5: track 21.8 -> 1.70 mm
- net /DDR3_ADDR7: track 15.8 -> 1.13 mm
- net /DDR3_ADDR9: track 15.5 -> 1.13 mm
- net /DDR3_DQ9: track 23.5 -> 9.31 mm
- net /DDR3_ADDR5: track 15.2 -> 1.13 mm
- net /DDR3_ADDR2: track 14.1 -> 1.13 mm
- net /DDR3_ADDR0: track 14.1 -> 1.70 mm
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- added copper zone on In4.Cu, net +1V5
